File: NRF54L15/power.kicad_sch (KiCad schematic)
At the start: 25 parts, among them IC2 BQ51013B, IC4 ST1PS02B1QTR

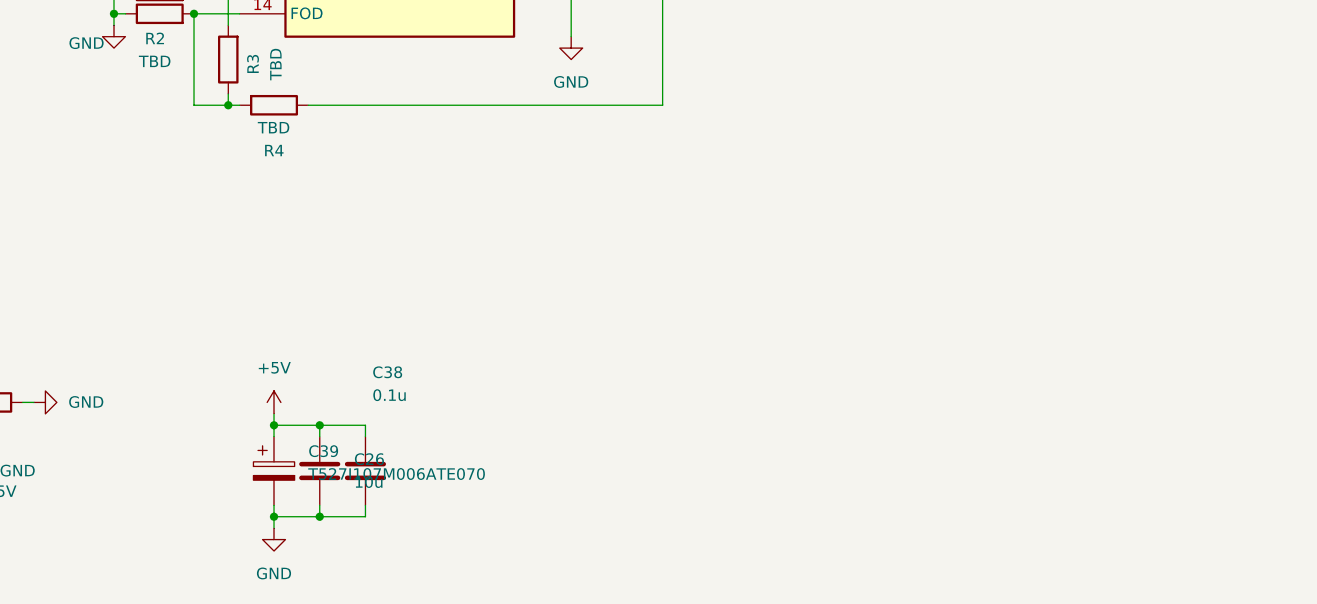
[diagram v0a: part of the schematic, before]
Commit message: nfc rect
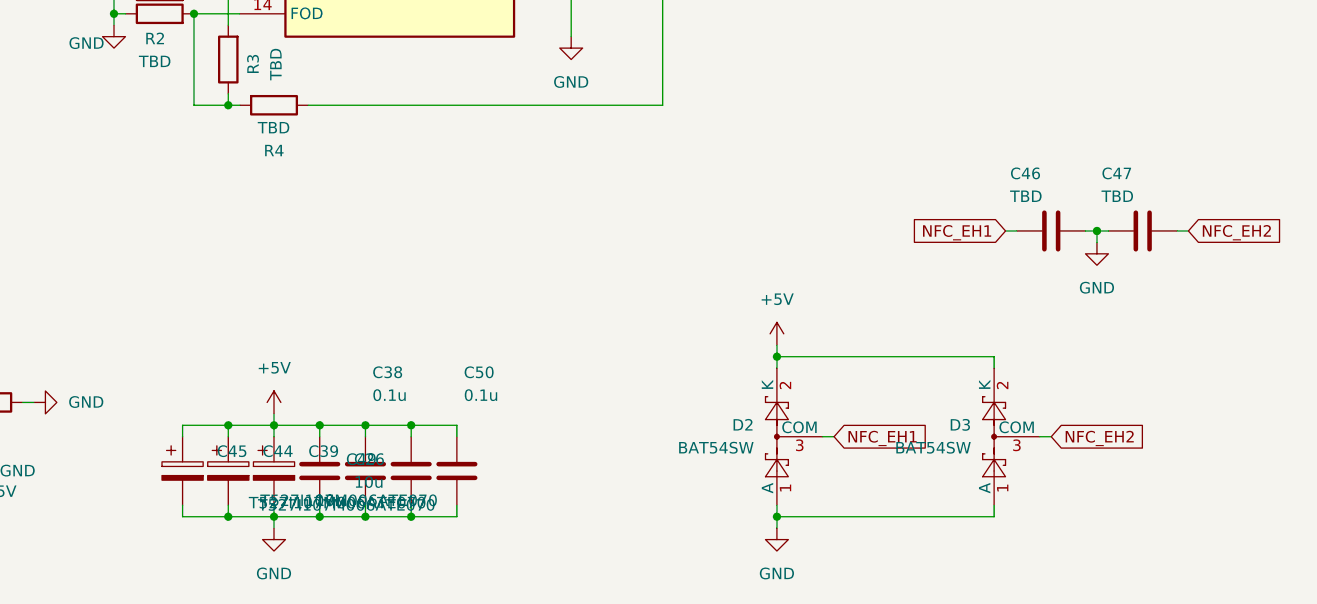
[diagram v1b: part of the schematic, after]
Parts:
- added C44, C45: T527I107M006ATE070, Capacitor_Tantalum_SMD:CP_EIA-3216-12_Kemet-S, symbol Device:C_Polarized
- added C46, C47: TBD, Capacitor_SMD:C_0201_0603Metric, symbol Device:C
- added C49: 10u, Capacitor_SMD:C_0402_1005Metric, symbol Device:C
- added C50: 0.1u, Capacitor_SMD:C_0201_0603Metric, symbol Device:C
- added D2, D3: BAT54SW, Package_TO_SOT_SMD:SOT-323_SC-70, symbol Diode:BAT54SW
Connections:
- net +5V: now also C44.1, C45.1, C49.1, C50.1, D2.2 (K), D3.2 (K)
- net GND: now also C44.2, C45.2, C46.2, C47.1, C49.2, C50.2, D2.1 (A), D3.1 (A)
- new net NFC_EH1: C46.1, D2.3 (COM)
- new net NFC_EH2: C47.2, D3.3 (COM)
